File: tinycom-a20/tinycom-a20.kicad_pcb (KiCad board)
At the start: 4 copper layers, 40.4 x 41.9 mm, 36 parts, among them P1 CONN_02X08, P2 CONN_02X08, U1 ALLWINNERA10/TFBGA441, U2 H5TQG63BFR/FBGA96, U3 H27UBG8T2A/TSOP48, Y1 Crystal_Small, Y2 Crystal_Small

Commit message: add power routes
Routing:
- net VCC_33: track 21.3 -> 204.1 mm, vias 12 -> 15
- net SVREF: track 6.25 -> 48.5 mm, vias 5 -> 6
- net UART0_TX: track 31.5 -> 0.00 mm
- net SDC0_D1: track 29.6 -> 0.00 mm, vias 1 -> 0
- net SDC0_D0: track 27.3 -> 0.00 mm, vias 1 -> 0
- net VCC_30: track 1.38 -> 27.4 mm
- net UART0_RX: track 25.7 -> 0.00 mm
- net SDC0_CMD: track 23.6 -> 0.00 mm, vias 1 -> 0
- net VCC_12: track 23.9 -> 45.6 mm
- net VCC_15: track 43.6 -> 62.7 mm
- net SDC0_CLK: track 15.9 -> 0.00 mm
- net SDC0_D2: track 12.0 -> 0.00 mm
- net SDC0_D3: track 11.2 -> 0.00 mm
- net GND: track 95.2 -> 99.6 mm
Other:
- net class Power: trace_width 0.15 -> 0.3
- rule pad_to_mask_clearance: 0.14 -> 0.2

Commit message: before autoroute remain
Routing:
- net SDC0_CMD: track 0.00 -> 8.93 mm
- net SDC0_CLK: track 0.00 -> 8.26 mm
- net SDC0_D1: track 0.00 -> 7.55 mm
- net SDC0_D0: track 0.00 -> 6.58 mm
- net NALE: track 17.3 -> 11.9 mm
- net UDM2: track 24.6 -> 27.9 mm
- net VCC_33: track 204.1 -> 201.2 mm
- net VCC_12: track 45.6 -> 48.3 mm
- net UDP2: track 29.0 -> 31.4 mm
- net SDC0_D3: track 0.00 -> 1.37 mm, vias 0 -> 1
- net SDC0_D2: track 0.00 -> 1.28 mm, vias 0 -> 1
- net GND: track 99.6 -> 98.5 mm, vias 44 -> 47
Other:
- rule pad_to_mask_clearance: 0.2 -> 0.14

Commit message: fixes
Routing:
- net UART0_RX: track 0.00 -> 65.3 mm
- net UART0_TX: track 0.00 -> 53.5 mm, vias 0 -> 1
- net SDC0_D1: track 7.55 -> 32.7 mm
- net SDC0_D0: track 6.58 -> 30.4 mm, vias 0 -> 2
- net VCC_33: track 201.2 -> 224.6 mm, vias 15 -> 16
- net SDC0_D3: track 1.37 -> 24.2 mm
- net SDC0_CLK: track 8.26 -> 28.7 mm, vias 0 -> 1
- net SDC0_D2: track 1.28 -> 21.5 mm, vias 1 -> 2
- net GND: track 98.5 -> 115.8 mm, vias 47 -> 48
- net SDC0_CMD: track 8.93 -> 24.2 mm, vias 0 -> 1
- net VCC_12: track 48.3 -> 62.8 mm
- net NRE#: track 15.1 -> 16.9 mm
- net ND2: track 11.8 -> 12.6 mm
- net NRB0: track 20.6 -> 21.3 mm
- net ND3: track 11.5 -> 12.2 mm
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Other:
- outline, holes or cut-outs redrawn

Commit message: fix
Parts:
- added C21: C_Small, Capacitors_SMD:C_0603, F.Cu at (105.3, 154.4)
- added C22: C_Small, Capacitors_SMD:C_0603, F.Cu at (103.9, 154.4)
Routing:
- net VCC_33: track 224.6 -> 231.1 mm, vias 16 -> 17
- net GND: track 115.8 -> 118.3 mm, vias 48 -> 50
- net VCC_12: track 62.8 -> 63.8 mm, vias 6 -> 7
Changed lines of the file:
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@@
 (kicad_pcb (version 4) (host pcbnew 4.0.0-rc1-stable)
   (general
-    (links 289)
-    (no_connects 4)
+    (links 293)
+    (no_connects 7)
     (area 84.760999 120.066999 125.297001 162.127001)
     (thickness 1.6)
     (drawings 18)
-    (tracks 2691)
+    (tracks 2711)
     (zones 0)
-    (modules 36)
+    (modules 38)
     (nets 92)
   )
@@
     )
   )
+  (module Capacitors_SMD:C_0603 (layer F.Cu)
+    (at 105.3084 154.4066 270)
+    (descr "Capacitor SMD 0603, reflow soldering, AVX (see smccp.pdf)")
+    (tags "capacitor 0603")
+    (attr smd)
+    (fp_text reference C21 (at 0 -1.9 270) (layer F.SilkS)
+      (effects (font (size 1 1) (thickness 0.15)))
+    )
+    (fp_text value C_Small (at 0 1.9 270) (layer F.Fab)
+      (effects (font (size 1 1) (thickness 0.15)))
+    )
+    (fp_line (start -1.45 -0.75) (end 1.45 -0.75) (layer F.CrtYd) (width 0.05))
+    (fp_line (start -1.45 0.75) (end 1.45 0.75) (layer F.CrtYd) (width 0.05))
+    (fp_line (start -1.45 -0.75) (end -1.45 0.75) (layer F.CrtYd) (width 0.05))
+    (fp_line (start 1.45 -0.75) (end 1.45 0.75) (layer F.CrtYd) (width 0.05))
+    (fp_line (start -0.35 -0.6) (end 0.35 -0.6) (layer F.SilkS) (width 0.15))
+    (fp_line (start 0.35 0.6) (end -0.35 0.6) (layer F.SilkS) (width 0.15))
+    (pad 1 smd rect (at -0.75 0 270) (size 0.8 0.75) (layers F.Cu F.Paste F.Mask)
+      (net 74 VCC_33))
+    (pad 2 smd rect (at 0.75 0 270) (size 0.8 0.75) (layers F.Cu F.Paste F.Mask)
+      (net 23 GND))
+    (model Capacitors_SMD.3dshapes/C_0603.wrl
+      (at (xyz 0 0 0))
+      (scale (xyz 1 1 1))
+      (rotate (xyz 0 0 0))
+    )
+  )
+  (module Capacitors_SMD:C_0603 (layer F.Cu)
+    (at 103.886 154.4066 270)
+    (descr "Capacitor SMD 0603, reflow soldering, AVX (see smccp.pdf)")
+    (tags "capacitor 0603")
+    (attr smd)
+    (fp_text reference C22 (at 0 -1.9 270) (layer F.SilkS)
+      (effects (font (size 1 1) (thickness 0.15)))
+    )
+    (fp_text value C_Small (at 0 1.9 270) (layer F.Fab)
+      (effects (font (size 1 1) (thickness 0.15)))
+    )
+    (fp_line (start -1.45 -0.75) (end 1.45 -0.75) (layer F.CrtYd) (width 0.05))
+    (fp_line (start -1.45 0.75) (end 1.45 0.75) (layer F.CrtYd) (width 0.05))
+    (fp_line (start -1.45 -0.75) (end -1.45 0.75) (layer F.CrtYd) (width 0.05))
+    (fp_line (start 1.45 -0.75) (end 1.45 0.75) (layer F.CrtYd) (width 0.05))
+    (fp_line (start -0.35 -0.6) (end 0.35 -0.6) (layer F.SilkS) (width 0.15))
+    (fp_line (start 0.35 0.6) (end -0.35 0.6) (layer F.SilkS) (width 0.15))
+    (pad 1 smd rect (at -0.75 0 270) (size 0.8 0.75) (layers F.Cu F.Paste F.Mask)
+      (net 72 VCC_12))
+    (pad 2 smd rect (at 0.75 0 270) (size 0.8 0.75) (layers F.Cu F.Paste F.Mask)
+      (net 23 GND))
+    (model Capacitors_SMD.3dshapes/C_0603.wrl
+      (at (xyz 0 0 0))
+      (scale (xyz 1 1 1))
+      (rotate (xyz 0 0 0))
+    )
+  )
   (gr_text TinyCom (at 93.3323 131.953) (layer F.SilkS)
     (effects (font (size 2 2) (thickness 0.5)))
@@
   (segment (start 107.3459 145.8471) (end 107.346 145.847) (width 0.15) (layer F.Cu) (net 22))
   (segment (start 107.3457 145.8471) (end 107.3459 145.8471) (width 0.15) (layer F.Cu) (net 22))
+  (segment (start 105.3084 155.1566) (end 105.3084 155.4988) (width 0.15) (layer F.Cu) (net 23))
+  (segment (start 105.3084 155.4988) (end 104.648 156.1592) (width 0.15) (layer F.Cu) (net 23))
+  (via (at 104.648 156.1592) (size 0.6) (drill 0.3) (layers F.Cu B.Cu) (net 23))
+  (segment (start 103.886 155.1566) (end 103.886 155.2956) (width 0.15) (layer F.Cu) (net 23))
+  (via (at 103.124 156.0576) (size 0.6) (drill 0.3) (layers F.Cu B.Cu) (net 23))
+  (segment (start 103.886 155.2956) (end 103.124 156.0576) (width 0.15) (layer F.Cu) (net 23))
   (via (at 85.85902 142.418) (size 0.6) (drill 0.3) (layers F.Cu B.Cu) (net 23))
   (segment (start 86.3624 142.443) (end 86.3374 142.418) (width 0.15) (layer F.Cu) (net 23))
@@
   (segment (start 116.2203 145.98) (end 116.326 145.98) (width 0.15) (layer F.Cu) (net 71))
   (segment (start 120.142 141.049) (end 120.142 141.046) (width 0.15) (layer F.Cu) (net 71))
+  (segment (start 105.9434 152.908) (end 110.5154 152.908) (width 0.3) (layer In2.Cu) (net 72))
+  (segment (start 105.0036 153.8478) (end 105.9434 152.908) (width 0.3) (layer In2.Cu) (net 72))
+  (segment (start 102.9208 153.8478) (end 105.0036 153.8478) (width 0.3) (layer In2.Cu) (net 72))
+  (segment (start 100.914 155.448) (end 101.3206 155.448) (width 0.3) (layer In2.Cu) (net 72))
+  (segment (start 101.3206 155.448) (end 102.620801 154.147799) (width 0.3) (layer In2.Cu) (net 72))
+  (segment (start 102.9208 153.8478) (end 102.620801 154.147799) (width 0.3) (layer In2.Cu) (net 72))
+  (segment (start 103.886 153.6566) (end 103.112 153.6566) (width 0.15) (layer F.Cu) (net 72))
+  (segment (start 103.112 153.6566) (end 102.9208 153.8478) (width 0.15) (layer F.Cu) (net 72))
+  (via (at 102.9208 153.8478) (size 0.6) (drill 0.3) (layers F.Cu B.Cu) (net 72))
   (segment (start 124.282 143.382) (end 123.47002 143.382) (width 0.15) (layer F.Cu) (net 72))
   (segment (start 123.47002 143.382) (end 123.43102 143.421) (width 0.15) (layer F.Cu) (net 72))
@@
   (segment (start 99.7379 156.624) (end 99.7379 159.046) (width 0.3) (layer In2.Cu) (net 72))
   (segment (start 100.914 155.448) (end 99.7379 156.624) (width 0.3) (layer In2.Cu) (net 72))
-  (segment (start 110.261 155.448) (end 100.914 155.448) (width 0.3) (layer In2.Cu) (net 72))
-  (segment (start 111.176 154.534) (end 110.261 155.448) (width 0.3) (layer In2.Cu) (net 72))
   (segment (start 119.098 151.866) (end 118.847 152.118) (width 0.15) (layer F.Cu) (net 72))
   (segment (start 120.129 151.866) (end 119.098 151.866) (width 0.15) (layer F.Cu) (net 72))
@@
   (segment (start 113.1105 144.6991) (end 112.5945 145.2151) (width 0.15) (layer F.Cu) (net 73))
   (segment (start 113.2829 144.6991) (end 113.1105 144.6991) (width 0.15) (layer F.Cu) (net 73))
+  (segment (start 104.818 158.834) (end 107.234647 158.834) (width 0.3) (layer In2.Cu) (net 74))
+  (segment (start 106.4006 153.7716) (end 107.145101 154.516101) (width 0.3) (layer In2.Cu) (net 74))
+  (segment (start 107.234647 158.834) (end 114.16 158.834) (width 0.3) (layer In2.Cu) (net 74))
+  (segment (start 107.145101 154.516101) (end 107.145101 158.744454) (width 0.3) (layer In2.Cu) (net 74))
+  (segment (start 107.145101 158.744454) (end 107.234647 158.834) (width 0.3) (layer In2.Cu) (net 74))
+  (segment (start 105.3084 153.6566) (end 106.2856 153.6566) (width 0.15) (layer F.Cu) (net 74))
+  (via (at 106.4006 153.7716) (size 0.6) (drill 0.3) (layers F.Cu B.Cu) (net 74))
+  (segment (start 106.2856 153.6566) (end 106.4006 153.7716) (width 0.15) (layer F.Cu) (net 74))
   (segment (start 104.724 128.702) (end 88.392 128.702) (width 0.3) (layer In2.Cu) (net 74))
   (segment (start 88.392 128.702) (end 86.0013 131.093) (width 0.3) (layer In2.Cu) (net 74))
@@
   (segment (start 85.471 153.3906) (end 86.3092 154.2288) (width 0.3) (layer In2.Cu) (net 74))
   (segment (start 85.471 143.661) (end 85.471 153.3906) (width 0.3) (layer In2.Cu) (net 74))
-  (segment (start 104.818 158.834) (end 114.16 158.834) (width 0.3) (layer In2.Cu) (net 74))
   (segment (start 114.16 158.834) (end 116.703 156.291) (width 0.3) (layer In2.Cu) (net 74))
   (segment (start 93.5482 153.5176) (end 94.3864 154.3558) (width 0.3) (layer In2.Cu) (net 74))

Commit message: readme
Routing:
- net VCC_33: track 231.1 -> 213.4 mm
- net VCC_12: track 63.8 -> 49.3 mm
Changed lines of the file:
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@@
   (general
     (links 293)
-    (no_connects 7)
-    (area 84.760999 120.066999 125.297001 162.127001)
+    (no_connects 4)
+    (area 83.32581 116.443 127.133 162.145001)
     (thickness 1.6)
     (drawings 18)
-    (tracks 2711)
+    (tracks 2700)
     (zones 0)
     (modules 38)
@@
   (segment (start 123.47002 143.382) (end 123.43102 143.421) (width 0.15) (layer F.Cu) (net 72))
   (via (at 123.43102 143.421) (size 0.6) (drill 0.3) (layers F.Cu B.Cu) (net 72))
-  (segment (start 101.765099 159.346401) (end 100.9015 160.21) (width 0.3) (layer B.Cu) (net 72))
-  (segment (start 102.1715 158.94) (end 101.765099 159.346401) (width 0.3) (layer B.Cu) (net 72))
-  (segment (start 103.8674 158.94) (end 102.1715 158.94) (width 0.3) (layer B.Cu) (net 72))
-  (segment (start 104.7052 158.1022) (end 103.8674 158.94) (width 0.3) (layer B.Cu) (net 72))
-  (segment (start 104.7052 157.0077) (end 104.7052 158.1022) (width 0.3) (layer B.Cu) (net 72))
-  (segment (start 110.8873 150.8256) (end 104.7052 157.0077) (width 0.3) (layer B.Cu) (net 72))
   (via (at 118.847 152.118) (size 0.6) (layers F.Cu B.Cu) (net 72))
   (via (at 109.728 131.204) (size 0.6) (layers F.Cu B.Cu) (net 72))
@@
   (segment (start 113.1105 144.6991) (end 112.5945 145.2151) (width 0.15) (layer F.Cu) (net 73))
   (segment (start 113.2829 144.6991) (end 113.1105 144.6991) (width 0.15) (layer F.Cu) (net 73))
+  (segment (start 107.234647 158.834) (end 114.16 158.834) (width 0.3) (layer In2.Cu) (net 74))
+  (segment (start 114.16 158.834) (end 115.2398 157.7542) (width 0.3) (layer In2.Cu) (net 74))
+  (segment (start 115.2398 157.7542) (end 115.2398 154.686) (width 0.3) (layer In2.Cu) (net 74))
+  (segment (start 115.8588 154.067) (end 116.703 154.067) (width 0.3) (layer In2.Cu) (net 74))
+  (segment (start 115.2398 154.686) (end 115.8588 154.067) (width 0.3) (layer In2.Cu) (net 74))
+  (segment (start 104.724 128.702) (end 102.779608 128.702) (width 0.3) (layer In2.Cu) (net 74))
+  (segment (start 102.779608 128.702) (end 88.392 128.702) (width 0.3) (layer In2.Cu) (net 74))
+  (segment (start 102.819 131.331) (end 102.819 128.741392) (width 0.3) (layer In2.Cu) (net 74))
+  (segment (start 102.819 128.741392) (end 102.779608 128.702) (width 0.3) (layer In2.Cu) (net 74))
   (segment (start 104.818 158.834) (end 107.234647 158.834) (width 0.3) (layer In2.Cu) (net 74))
   (segment (start 106.4006 153.7716) (end 107.145101 154.516101) (width 0.3) (layer In2.Cu) (net 74))
-  (segment (start 107.234647 158.834) (end 114.16 158.834) (width 0.3) (layer In2.Cu) (net 74))
   (segment (start 107.145101 154.516101) (end 107.145101 158.744454) (width 0.3) (layer In2.Cu) (net 74))
   (segment (start 107.145101 158.744454) (end 107.234647 158.834) (width 0.3) (layer In2.Cu) (net 74))
@@
   (via (at 106.4006 153.7716) (size 0.6) (drill 0.3) (layers F.Cu B.Cu) (net 74))
   (segment (start 106.2856 153.6566) (end 106.4006 153.7716) (width 0.15) (layer F.Cu) (net 74))
-  (segment (start 104.724 128.702) (end 88.392 128.702) (width 0.3) (layer In2.Cu) (net 74))
   (segment (start 88.392 128.702) (end 86.0013 131.093) (width 0.3) (layer In2.Cu) (net 74))
   (segment (start 86.0013 131.093) (end 86.0013 141.687078) (width 0.3) (layer In2.Cu) (net 74))
@@
   (segment (start 86.0013 141.687078) (end 86.449021 142.134799) (width 0.3) (layer In2.Cu) (net 74))
   (segment (start 86.449021 142.682979) (end 85.471 143.661) (width 0.3) (layer In2.Cu) (net 74))
-  (segment (start 116.703 156.291) (end 116.703 154.067) (width 0.3) (layer In2.Cu) (net 74))
   (segment (start 85.471 153.3906) (end 86.3092 154.2288) (width 0.3) (layer In2.Cu) (net 74))
   (segment (start 85.471 143.661) (end 85.471 153.3906) (width 0.3) (layer In2.Cu) (net 74))
-  (segment (start 114.16 158.834) (end 116.703 156.291) (width 0.3) (layer In2.Cu) (net 74))
   (segment (start 93.5482 153.5176) (end 94.3864 154.3558) (width 0.3) (layer In2.Cu) (net 74))
   (segment (start 91.6686 153.5176) (end 93.5482 153.5176) (width 0.3) (layer In2.Cu) (net 74))
@@
   (segment (start 120.116 153.521) (end 119.396 152.801) (width 0.15) (layer B.Cu) (net 74))
   (segment (start 120.116 153.721) (end 120.116 153.521) (width 0.15) (layer B.Cu) (net 74))
-  (segment (start 102.819 130.607) (end 104.724 128.702) (width 0.3) (layer In2.Cu) (net 74))
-  (segment (start 102.819 131.331) (end 102.819 130.607) (width 0.3) (layer In2.Cu) (net 74))
   (segment (start 123.182 146.896) (end 123.482 146.596) (width 0.3) (layer In2.Cu) (net 74))
   (segment (start 123.062 147.017) (end 123.182 146.896) (width 0.3) (layer In2.Cu) (net 74))
@@
   (segment (start 119.342 149.047) (end 119.342 149.035) (width 0.15) (layer F.Cu) (net 74))
   (segment (start 119.342 138.651) (end 119.342 138.283) (width 0.15) (layer F.Cu) (net 74))
-  (segment (start 105.334 128.092) (end 104.724 128.702) (width 0.3) (layer In2.Cu) (net 74))
   (segment (start 119.232 153.225) (end 118.39 154.067) (width 0.3) (layer In2.Cu) (net 74))
   (segment (start 119.232 152.801) (end 119.232 153.225) (width 0.3) (layer In2.Cu) (net 74))
@@
   (segment (start 118.677 148.912) (end 118.948 148.641) (width 0.15) (layer B.Cu) (net 74))
   (segment (start 118.677 150.5687) (end 118.677 148.912) (width 0.15) (layer B.Cu) (net 74))
-  (segment (start 115.8418 153.772) (end 116.713 153.772) (width 0.3) (layer B.Cu) (net 74))
-  (segment (start 112.3315 157.2823) (end 115.8418 153.772) (width 0.3) (layer B.Cu) (net 74))
-  (segment (start 112.3315 158.0991) (end 112.3315 157.2823) (width 0.3) (layer B.Cu) (net 74))
-  (segment (start 111.3845 159.0461) (end 112.3315 158.0991) (width 0.3) (layer B.Cu) (net 74))
-  (segment (start 105.4782 159.0461) (end 111.3845 159.0461) (width 0.3) (layer B.Cu) (net 74))
-  (segment (start 104.6054 159.9189) (end 105.4782 159.0461) (width 0.3) (layer B.Cu) (net 74))
-  (segment (start 104.6054 160.21) (end 104.6054 159.9189) (width 0.3) (layer B.Cu) (net 74))
-  (segment (start 103.4415 160.21) (end 104.6054 160.21) (width 0.3) (layer B.Cu) (net 74))
   (segment (start 116.142 140.2512) (end 116.142 140.251) (width 0.3) (layer F.Cu) (net 74))
   (segment (start 116.1418 140.2514) (end 116.142 140.2512) (width 0.3) (layer F.Cu) (net 74))
@@
   (segment (start 115.816 139.926) (end 115.816 139.126) (width 0.15) (layer F.Cu) (net 74))
   (segment (start 116.142 140.251) (end 115.816 139.926) (width 0.15) (layer F.Cu) (net 74))
-  (segment (start 117.5512 137.9728) (end 117.654484 137.9728) (width 0.15) (layer B.Cu) (net 75))
+  (segment (start 118.177025 138.495341) (end 119.75468 140.072996) (width 0.15) (layer B.Cu) (net 75))
+  (segment (start 117.047351 138.476649) (end 118.158333 138.476649) (width 0.15) (layer B.Cu) (net 75))
+  (segment (start 112.413202 143.110798) (end 117.047351 138.476649) (width 0.15) (layer B.Cu) (net 75))
+  (segment (start 118.158333 138.476649) (end 118.177025 138.495341) (width 0.15) (layer B.Cu) (net 75))
   (segment (start 119.75468 140.072996) (end 119.75468 140.234553) (width 0.15) (layer B.Cu) (net 75))
   (segment (start 111.5314 152.1201) (end 111.5314 148.817074) (width 0.15) (layer B.Cu) (net 75))
-  (segment (start 117.654484 137.9728) (end 119.75468 140.072996) (width 0.15) (layer B.Cu) (net 75))
   (segment (start 111.5314 148.817074) (end 112.413202 147.935272) (width 0.15) (layer B.Cu) (net 75))
   (segment (start 105.9815 157.67) (end 111.5314 152.1201) (width 0.15) (layer B.Cu) (net 75))
   (segment (start 112.413202 147.935272) (end 112.413202 143.110798) (width 0.15) (layer B.Cu) (net 75))
   (segment (start 119.75468 140.234553) (end 119.75468 140.658817) (width 0.15) (layer B.Cu) (net 75))
-  (segment (start 112.413202 143.110798) (end 117.5512 137.9728) (width 0.15) (layer B.Cu) (net 75))
   (segment (start 120.14226 140.25144) (end 120.14226 140.271237) (width 0.15) (layer F.Cu) (net 75))
   (segment (start 120.14226 140.271237) (end 119.75468 140.658817) (width 0.15) (layer F.Cu) (net 75))

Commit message: pic
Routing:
- net GND: track 118.3 -> 178.4 mm
- net UART0_RX: track 65.3 -> 5.11 mm

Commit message: update base board
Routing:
- net UART0_RX: track 5.11 -> 65.3 mm
- net GND: track 178.4 -> 118.3 mm
- net SDC0_D0: track 30.4 -> 28.6 mm
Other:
- net class Default: clearance 0.15 -> 0.14
- net class Ground: clearance 0.15 -> 0.14
- net class Power: clearance 0.15 -> 0.14
- rule pad_to_mask_clearance: 0.14 -> 0.07
- rule trace_clearance: 0.15 -> 0.14

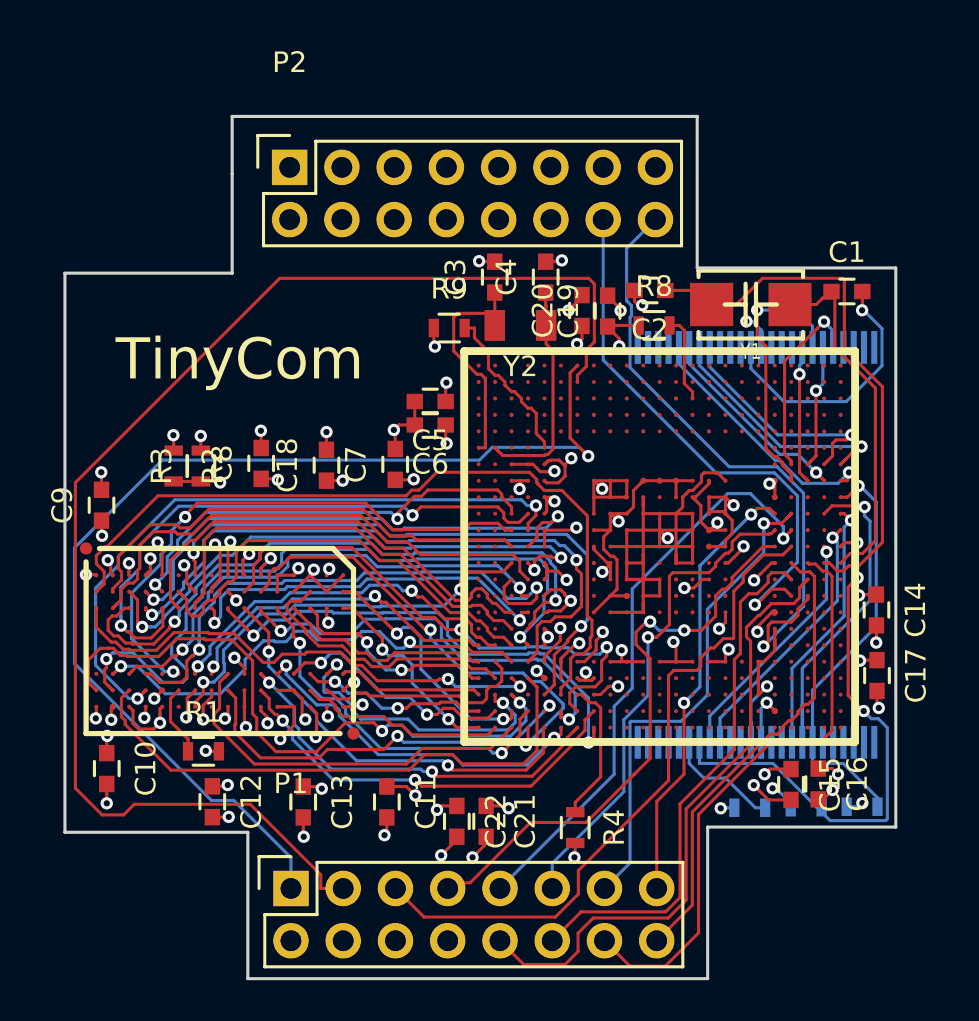
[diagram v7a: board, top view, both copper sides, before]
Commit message: add uboot_sel test point
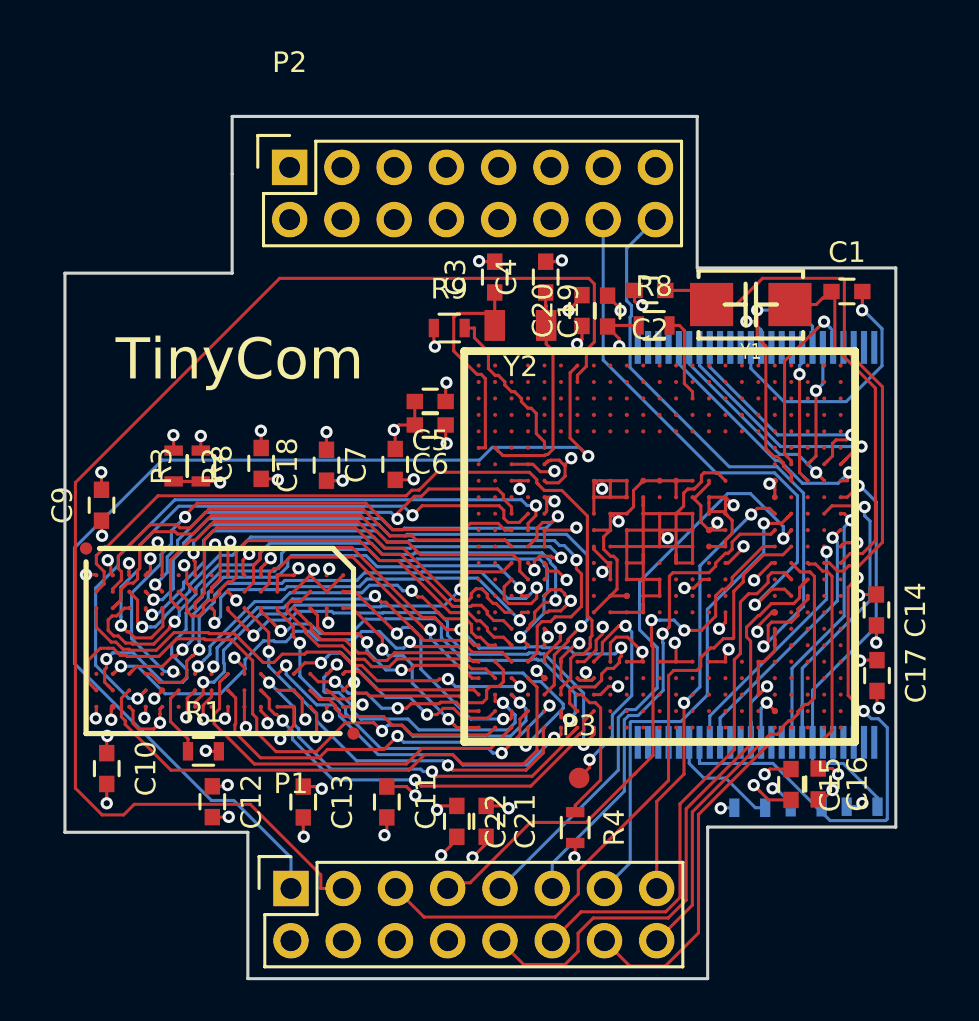
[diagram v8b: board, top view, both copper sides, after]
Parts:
- added P3: CONN_01X01, tinycom:tc-Measurement_Point_Round-SMD-Pad_Small, F.Cu at (109.8, 152.3)
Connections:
- net Net-(R8-Pad2) renamed RESET#
- net Net-(R9-Pad2) renamed NMI#
- U1 pad W8: (no net) -> UBOOT_SEL
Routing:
- net UBOOT_SEL: track 0.00 -> 11.1 mm, vias 0 -> 2
- net GND: track 118.3 -> 120.4 mm
- net SDQ6: track 26.1 -> 27.2 mm
- net SDC0_CLK: track 28.3 -> 29.3 mm
- net SDC0_D0: track 28.6 -> 28.0 mm
